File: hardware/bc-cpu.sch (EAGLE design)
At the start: 6 parts, among them U1 R-735.0P

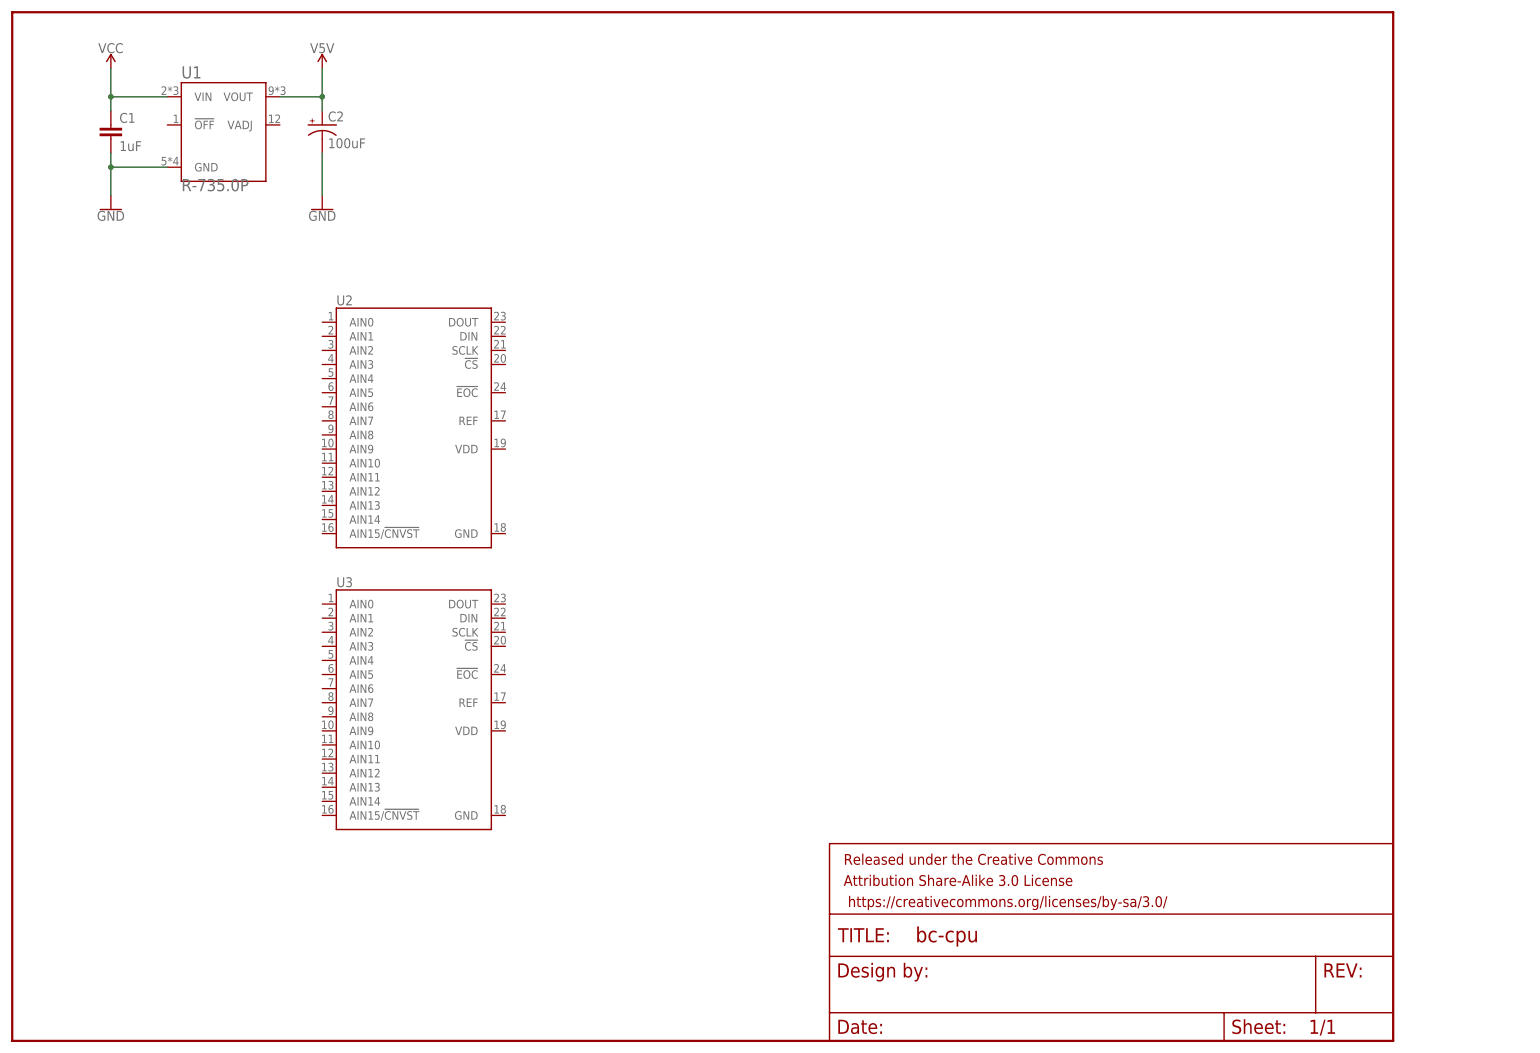
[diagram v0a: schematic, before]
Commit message: Added resistors array
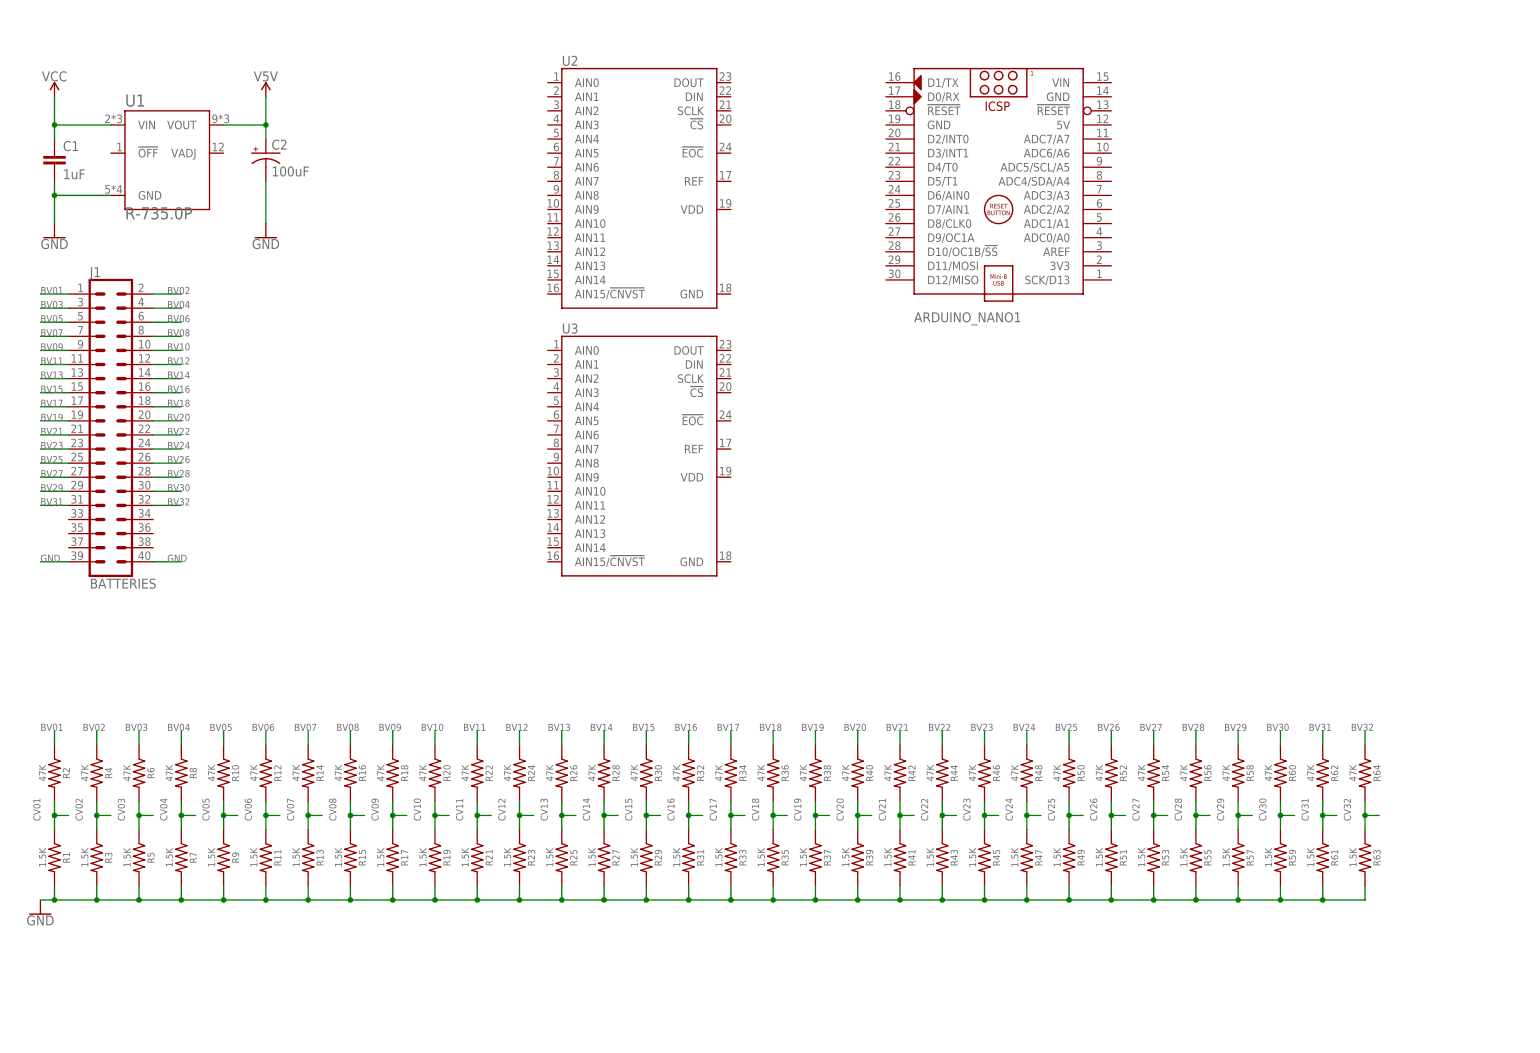
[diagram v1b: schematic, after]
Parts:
- removed FRAME1: FRAME-LETTER, SparkFun-Retired:FRAME-LETTER
- added ARDUINO_NANO1: (no value), ArduinoNanoV30:ARDUINO_NANO
- added J1: BATTERIES, SparkFun-Connectors:CONN_20X2SHROUDED
- added R1, R11, R13, R15, R17, R19, R21, R23, R25, R27, R29, R3, R31, R33, R35, R37, R39, R41, R43, R45, R47, R49, R5, R51, R53, R55, R57, R59, R61, R63, R7, R9: 1.5K, SparkFun-Resistors:RESISTOR1206
- added R10, R12, R14, R16, R18, R2, R20, R22, R24, R26, R28, R30, R32, R34, R36, R38, R4, R40, R42, R44, R46, R48, R50, R52, R54, R56, R58, R6, R60, R62, R64, R8: 47K, SparkFun-Resistors:RESISTOR1206
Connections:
- new net BV01: J1.1, R2.1
- new net BV02: J1.2, R4.1
- new net BV03: J1.3, R6.1
- new net BV04: J1.4, R8.1
- new net BV05: J1.5, R10.1
- new net BV06: J1.6, R12.1
- new net BV07: J1.7, R14.1
- new net BV08: J1.8, R16.1
- new net BV09: J1.9, R18.1
- new net BV10: J1.10, R20.1
- new net BV11: J1.11, R22.1
- new net BV12: J1.12, R24.1
- new net BV13: J1.13, R26.1
- new net BV14: J1.14, R28.1
- new net BV15: J1.15, R30.1
- new net BV16: J1.16, R32.1
- new net BV17: J1.17, R34.1
- new net BV18: J1.18, R36.1
- new net BV19: J1.19, R38.1
- new net BV20: J1.20, R40.1
- new net BV21: J1.21, R42.1
- new net BV22: J1.22, R44.1
- new net BV23: J1.23, R46.1
- new net BV24: J1.24, R48.1
- new net BV25: J1.25, R50.1
- new net BV26: J1.26, R52.1
- new net BV27: J1.27, R54.1
- new net BV28: J1.28, R56.1
- new net BV29: J1.29, R58.1
- new net BV30: J1.30, R60.1
- new net BV31: J1.31, R62.1
- new net BV32: J1.32, R64.1
- new net CV01: R1.1, R2.2
- new net CV02: R3.1, R4.2
- new net CV03: R5.1, R6.2
- new net CV04: R7.1, R8.2
- new net CV05: R10.2, R9.1
- new net CV06: R11.1, R12.2
- new net CV07: R13.1, R14.2
- new net CV08: R15.1, R16.2
- new net CV09: R17.1, R18.2
- new net CV10: R19.1, R20.2
- new net CV11: R21.1, R22.2
- new net CV12: R23.1, R24.2
- new net CV13: R25.1, R26.2
- new net CV14: R27.1, R28.2
- new net CV15: R29.1, R30.2
- new net CV16: R31.1, R32.2
- new net CV17: R33.1, R34.2
- new net CV18: R35.1, R36.2
- new net CV19: R37.1, R38.2
- new net CV20: R39.1, R40.2
- new net CV21: R41.1, R42.2
- new net CV22: R43.1, R44.2
- new net CV23: R45.1, R46.2
- new net CV24: R47.1, R48.2
- new net CV25: R49.1, R50.2
- new net CV26: R51.1, R52.2
- new net CV27: R53.1, R54.2
- new net CV28: R55.1, R56.2
- new net CV29: R57.1, R58.2
- new net CV30: R59.1, R60.2
- new net CV31: R61.1, R62.2
- new net CV32: R63.1, R64.2
- net GND: now also J1.39, J1.40, R1.2, R11.2, R13.2, R15.2, R17.2, R19.2, R21.2, R23.2, R25.2, R27.2, R29.2, R3.2, R31.2, R33.2, R35.2, R37.2, R39.2, R41.2, R43.2, R45.2, R47.2, R49.2, R5.2, R51.2, R53.2, R55.2, R57.2, R59.2, R61.2, R63.2, R7.2, R9.2
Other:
- moved on the sheet: C1, C2, U1, U2, U3

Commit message: Added voltage reference
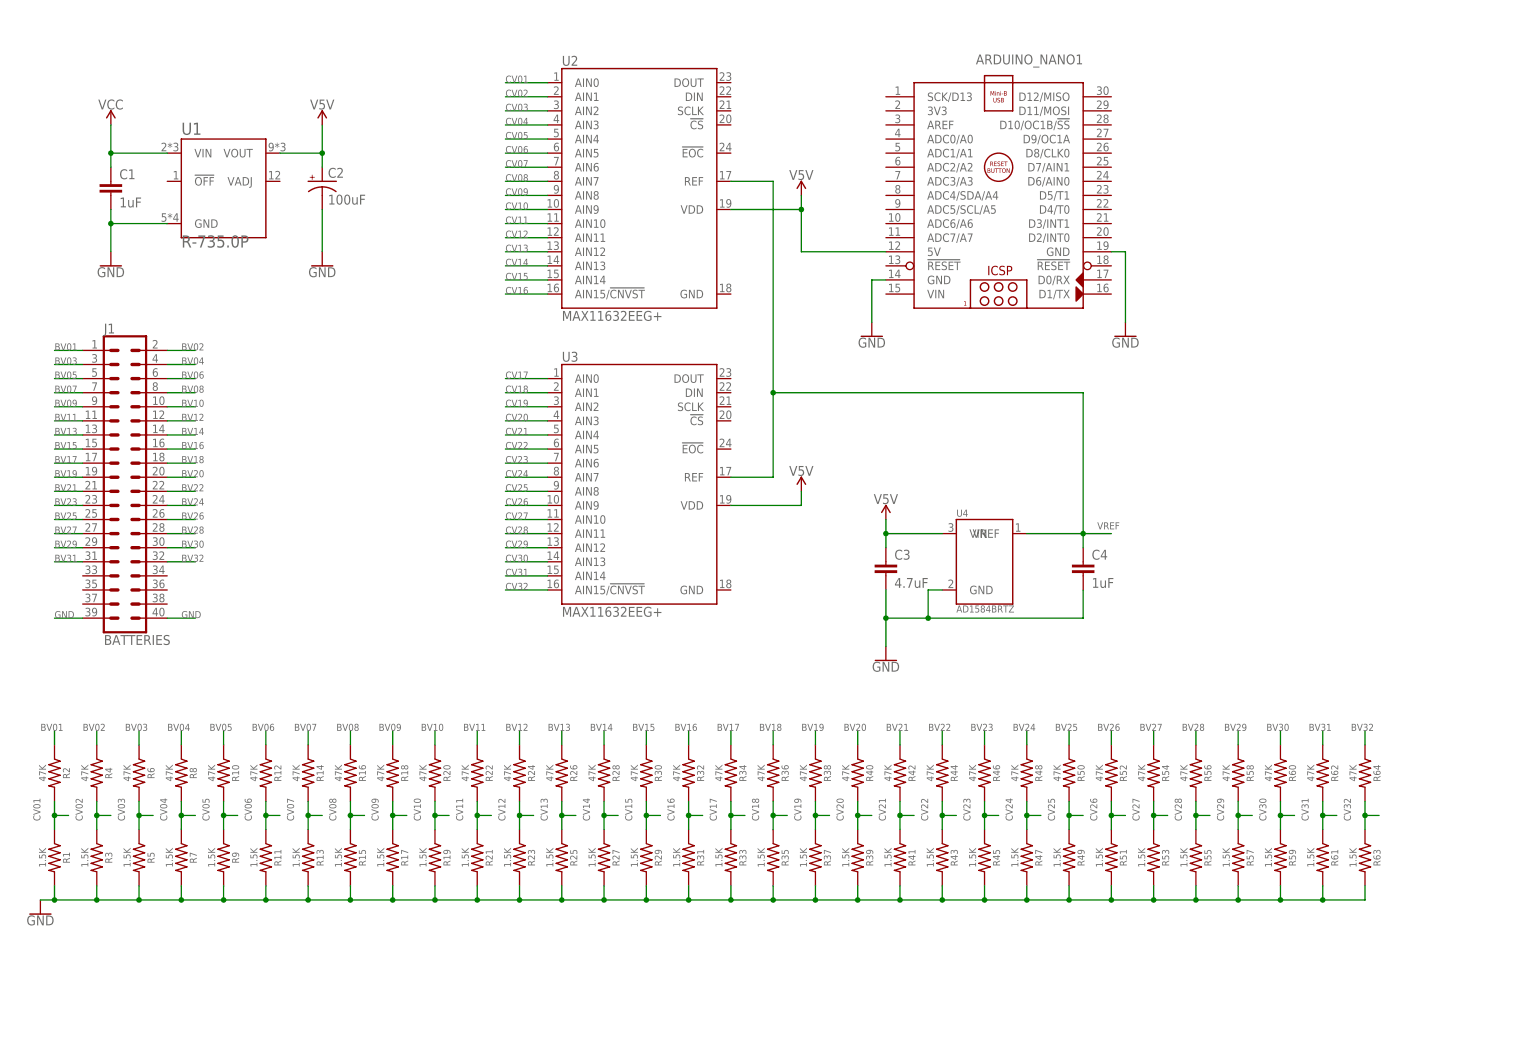
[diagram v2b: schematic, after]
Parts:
- added C3: 4.7uF, capacitor-wima:C5/3
- added C4: 1uF, capacitor-wima:C5/3
- added U4: AD1584BRTZ, VREF-AD1582-85:AD1582
- U2, U3: value (none) -> MAX11632EEG+
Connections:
- new net VCC_1: ARDUINO_NANO1.5V, C3.1, U2.VDD, U3.VDD, U4.VIN
- new net VREF: C4.1, U2.REF, U3.REF, U4.VREF
- net CV01: now also U2.AIN0
- net CV02: now also U2.AIN1
- net CV03: now also U2.AIN2
- net CV04: now also U2.AIN3
- net CV05: now also U2.AIN4
- net CV06: now also U2.AIN5
- net CV07: now also U2.AIN6
- net CV08: now also U2.AIN7
- net CV09: now also U2.AIN8
- net CV10: now also U2.AIN9
- net CV11: now also U2.AIN10
- net CV12: now also U2.AIN11
- net CV13: now also U2.AIN12
- net CV14: now also U2.AIN13
- net CV15: now also U2.AIN14
- net CV16: now also U2.AIN15/!CNVST
- net CV17: now also U3.AIN0
- net CV18: now also U3.AIN1
- net CV19: now also U3.AIN2
- net CV20: now also U3.AIN3
- net CV21: now also U3.AIN4
- net CV22: now also U3.AIN5
- net CV23: now also U3.AIN6
- net CV24: now also U3.AIN7
- net CV25: now also U3.AIN8
- net CV26: now also U3.AIN9
- net CV27: now also U3.AIN10
- net CV28: now also U3.AIN11
- net CV29: now also U3.AIN12
- net CV30: now also U3.AIN13
- net CV31: now also U3.AIN14
- net CV32: now also U3.AIN15/!CNVST
- net GND: now also ARDUINO_NANO1.GND@1, ARDUINO_NANO1.GND@2, C3.2, C4.2, U4.GND
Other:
- moved on the sheet: ARDUINO_NANO1, C1, C2, J1, U1, U3

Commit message: Final schematic, before PCB
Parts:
- added C5, C6, C7, C8: 0.1uF, capacitor-wima:C5/3
- added J2: (no value), SparkFun-Connectors:CONN_02
- added J3: (no value), SparkFun-Connectors:CONN_05X2SHD
- added J4: 12V, SparkFun-Connectors:CONN_02
- added J5: 5V, SparkFun-Connectors:CONN_02
- added R65: 10K, SparkFun-Resistors:RESISTOR1206
- added S1: (no value), SparkFun-Switches:DIP-08-PTH
- renumbered ARDUINO_NANO1 to ARDUINO_NANO
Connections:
- removed net VCC_1: ARDUINO_NANO.5V, C3.1, U2.VDD, U3.VDD, U4.VIN
- new net CS0: ARDUINO_NANO.D10/OC1B/!SS, U2.!CS
- new net CS1: ARDUINO_NANO.D9/OC1A, U3.!CS
- new net LEDCLK: ARDUINO_NANO.ADC5/SCL/A5, J3.1, J3.2
- new net LEDDAT: ARDUINO_NANO.ADC4/SDA/A4, J3.3, J3.4
- new net MISO: ARDUINO_NANO.D12/MISO, U2.DOUT, U3.DOUT
- new net MOSI: ARDUINO_NANO.D11/MOSI, U2.DIN, U3.DIN
- new net N$1: ARDUINO_NANO.D2/INT0, S1.16
- new net N$10: C1.1, J4.1, U1.VIN
- new net N$11: C2.+, J5.1, U1.VOUT
- new net N$2: C7.1, U3.REF
- new net N$3: C8.1, U2.REF
- new net N$4: ARDUINO_NANO.D3/INT1, S1.15
- new net N$5: ARDUINO_NANO.D4/T0, S1.14
- new net N$6: ARDUINO_NANO.D5/T1, S1.13
- new net N$7: ARDUINO_NANO.D6/AIN0, S1.12
- new net N$8: ARDUINO_NANO.D7/AIN1, S1.11
- new net N$9: ARDUINO_NANO.D8/CLK0, S1.10
- new net PHOTO: J2.1, J3.10, J3.9, R65.1
- new net SCLK: ARDUINO_NANO.SCK/D13, U2.SCLK, U3.SCLK
- net GND: now also C5.2, C6.2, C7.2, C8.2, J3.5, J3.6, R65.2, S1.1, S1.2, S1.3, S1.4, S1.5, S1.6, S1.7, S1.8, U2.GND, U3.GND
- net V5V: now also ARDUINO_NANO.5V, C3.1, C5.1, C6.1, J2.2, J3.7, J3.8, J5.2, U2.VDD, U3.VDD, U4.VIN; no longer C2.+, U1.VOUT
- net VCC: now also J4.2; no longer C1.1, U1.VIN
- net VREF: no longer U2.REF, U3.REF
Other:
- note added: "LED Matrix"
- note added: "Photo Resistor (Light Sensor)"
- moved on the sheet: C1, C2, C3, C4, J1, U1, U2, U3, U4

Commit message: The initial rats nest
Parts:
- J2: value (none) -> PHT
- J3: value (none) -> LED Matrix
- S1: value (none) -> Options
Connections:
- net N$1 renamed DIP1
- net N$4 renamed DIP2
- net N$5 renamed DIP3
- net N$6 renamed DIP4
- net N$7 renamed DIP5
- net N$8 renamed DIP6
- net N$9 renamed DIP7
- new net DIP8: ARDUINO_NANO.ADC7/A7, S1.9
- new net EOC0: ARDUINO_NANO.ADC0/A0, U2.!EOC
- new net EOC1: ARDUINO_NANO.ADC1/A1, U3.!EOC
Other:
- note removed: "LED Matrix"
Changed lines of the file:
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@@
 <part name="GND8" library="SparkFun-PowerSymbols" deviceset="GND" device=""/>
 <part name="V5V4" library="SparkFun-PowerSymbols" deviceset="VCC_1" device="" value="V5V"/>
-<part name="J3" library="SparkFun-Connectors" deviceset="CONN_05X2" device="SHD"/>
-<part name="S1" library="SparkFun-Switches" deviceset="DIP-08" device="-PTH"/>
+<part name="J3" library="SparkFun-Connectors" deviceset="CONN_05X2" device="SHD" value="LED Matrix"/>
+<part name="S1" library="SparkFun-Switches" deviceset="DIP-08" device="-PTH" value="Options"/>
 <part name="GND9" library="SparkFun-PowerSymbols" deviceset="GND" device=""/>
 <part name="R65" library="SparkFun-Resistors" deviceset="RESISTOR" device="1206" value="10K"/>
 <part name="GND10" library="SparkFun-PowerSymbols" deviceset="GND" device=""/>
-<part name="J2" library="SparkFun-Connectors" deviceset="CONN_02" device=""/>
+<part name="J2" library="SparkFun-Connectors" deviceset="CONN_02" device="" value="PHT"/>
 <part name="J4" library="SparkFun-Connectors" deviceset="CONN_02" device="" value="12V"/>
 <part name="J5" library="SparkFun-Connectors" deviceset="CONN_02" device="" value="5V"/>
@@
 <sheet>
 <plain>
-<text x="251.46" y="101.6" size="1.778" layer="91">Photo Resistor
+<text x="246.38" y="101.6" size="1.778" layer="91">Photo Resistor
 (Light Sensor)</text>
-<text x="243.84" y="152.4" size="1.778" layer="91">LED Matrix</text>
 </plain>
 <instances>
@@
 <pinref part="U3" gate="U1" pin="DIN"/>
 <wire x1="116.84" y1="114.3" x2="124.46" y2="114.3" width="0.1524" layer="91"/>
+<label x="121.92" y="114.3" size="1.778" layer="95"/>
 </segment>
 <segment>
@@
 <wire x1="116.84" y1="116.84" x2="124.46" y2="116.84" width="0.1524" layer="91"/>
 <label x="121.92" y="116.84" size="1.778" layer="95"/>
-<label x="121.92" y="114.3" size="1.778" layer="95"/>
 </segment>
 <segment>
@@
 </segment>
 </net>
-<net name="N$1" class="0">
+<net name="DIP1" class="0">
 <segment>
 <pinref part="ARDUINO_NANO" gate="G$1" pin="D2/INT0"/>
@@
 </segment>
 </net>
-<net name="N$4" class="0">
+<net name="DIP2" class="0">
 <segment>
 <pinref part="ARDUINO_NANO" gate="G$1" pin="D3/INT1"/>
@@
 </segment>
 </net>
-<net name="N$5" class="0">
+<net name="DIP3" class="0">
 <segment>
 <pinref part="ARDUINO_NANO" gate="G$1" pin="D4/T0"/>
@@
 </segment>
 </net>
-<net name="N$6" class="0">
+<net name="DIP4" class="0">
 <segment>
 <pinref part="ARDUINO_NANO" gate="G$1" pin="D5/T1"/>
@@
 </segment>
 </net>
-<net name="N$7" class="0">
+<net name="DIP5" class="0">
 <segment>
 <pinref part="ARDUINO_NANO" gate="G$1" pin="D6/AIN0"/>
@@
 </segment>
 </net>
-<net name="N$8" class="0">
+<net name="DIP6" class="0">
 <segment>
 <pinref part="ARDUINO_NANO" gate="G$1" pin="D7/AIN1"/>
@@
 </segment>
 </net>
-<net name="N$9" class="0">
+<net name="DIP7" class="0">
 <segment>
 <pinref part="ARDUINO_NANO" gate="G$1" pin="D8/CLK0"/>
@@
 </segment>
 </net>
+<net name="EOC0" class="0">
+<segment>
+<pinref part="U2" gate="U1" pin="!EOC"/>
+<wire x1="116.84" y1="157.48" x2="124.46" y2="157.48" width="0.1524" layer="91"/>
+<label x="121.92" y="157.48" size="1.778" layer="95"/>
+</segment>
+<segment>
+<pinref part="ARDUINO_NANO" gate="G$1" pin="ADC0/A0"/>
+<wire x1="157.48" y1="162.56" x2="149.86" y2="162.56" width="0.1524" layer="91"/>
+<label x="149.86" y="162.56" size="1.778" layer="95"/>
+</segment>
+</net>
+<net name="EOC1" class="0">
+<segment>
+<pinref part="U3" gate="U1" pin="!EOC"/>
+<wire x1="116.84" y1="104.14" x2="124.46" y2="104.14" width="0.1524" layer="91"/>
+<label x="121.92" y="104.14" size="1.778" layer="95"/>
+</segment>
+<segment>
+<pinref part="ARDUINO_NANO" gate="G$1" pin="ADC1/A1"/>
+<wire x1="157.48" y1="160.02" x2="149.86" y2="160.02" width="0.1524" layer="91"/>
+<label x="149.86" y="160.02" size="1.778" layer="95"/>
+</segment>
+</net>
+<net name="DIP8" class="0">
+<segment>
+<pinref part="ARDUINO_NANO" gate="G$1" pin="ADC7/A7"/>
+<wire x1="157.48" y1="144.78" x2="149.86" y2="144.78" width="0.1524" layer="91"/>
+<label x="149.86" y="144.78" size="1.778" layer="95"/>
+</segment>
+<segment>
+<pinref part="S1" gate="A" pin="9"/>
+<wire x1="231.14" y1="132.08" x2="231.14" y2="139.7" width="0.1524" layer="91"/>
+<label x="231.14" y="137.16" size="1.778" layer="95"/>
+</segment>
+</net>
 </nets>
 </sheet>
 </sheets>
+<errors>
+</errors>
 </schematic>
 </drawing>

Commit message: Layout attempt with SMD MAX-11632
Lots of random traces that need to be placed by hand. Committing before
trying a different approach.
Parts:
- removed J4: 12V, SparkFun-Connectors:CONN_02
- added POWER: 12V, SparkFun-Connectors:CONN_02
- J5: value 5V -> BRK5
- R65: value 10K -> (none); device SparkFun-Resistors:RESISTOR1206 -> SparkFun-Resistors:RESISTORAXIAL-0.3
- U2, U3: device MAX-11632:MAX-11632ADPT24W30 -> MAX-11632:MAX-11632QSOP24
- renumbered C5 to C22, C6 to C32, C7 to C31, C8 to C21
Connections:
- removed net N$10: C1.1, J4.1, U1.VIN
- net GND: now also POWER.1
- net VCC: now also C1.1, POWER.2, U1.VIN; no longer J4.2
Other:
- moved on the sheet: C1, C2, J5, U1

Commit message: Fixed VREF bug, mostly routed
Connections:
- removed net N$2: C31.1, U3.REF
- removed net N$3: C21.1, U2.REF
- net VREF: now also C21.1, C31.1, U2.REF, U3.REF
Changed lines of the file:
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@@
 <label x="200.66" y="92.202" size="1.27" layer="95"/>
 </segment>
-</net>
-<net name="N$2" class="0">
+<segment>
+<pinref part="U2" gate="U1" pin="REF"/>
+<wire x1="124.46" y1="152.4" x2="119.38" y2="152.4" width="0.1524" layer="91"/>
+<pinref part="C21" gate="G$1" pin="1"/>
+<wire x1="119.38" y1="152.4" x2="116.84" y2="152.4" width="0.1524" layer="91"/>
+<wire x1="119.38" y1="152.4" x2="119.38" y2="142.24" width="0.1524" layer="91"/>
+<junction x="119.38" y="152.4"/>
+<label x="121.92" y="152.4" size="1.778" layer="95"/>
+</segment>
 <segment>
 <pinref part="U3" gate="U1" pin="REF"/>
@@
 <wire x1="119.38" y1="88.9" x2="119.38" y2="99.06" width="0.1524" layer="91"/>
 <junction x="119.38" y="99.06"/>
+<label x="121.92" y="99.06" size="1.778" layer="95"/>
 </segment>
 </net>
-<net name="N$3" class="0">
-<segment>
-<pinref part="U2" gate="U1" pin="REF"/>
-<wire x1="124.46" y1="152.4" x2="119.38" y2="152.4" width="0.1524" layer="91"/>
-<pinref part="C21" gate="G$1" pin="1"/>
-<wire x1="119.38" y1="152.4" x2="116.84" y2="152.4" width="0.1524" layer="91"/>
-<wire x1="119.38" y1="152.4" x2="119.38" y2="142.24" width="0.1524" layer="91"/>
-<junction x="119.38" y="152.4"/>
-</segment>
-</net>
